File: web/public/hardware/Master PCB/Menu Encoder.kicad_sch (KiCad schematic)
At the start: 7 parts, among them SW2 Menu Encoder

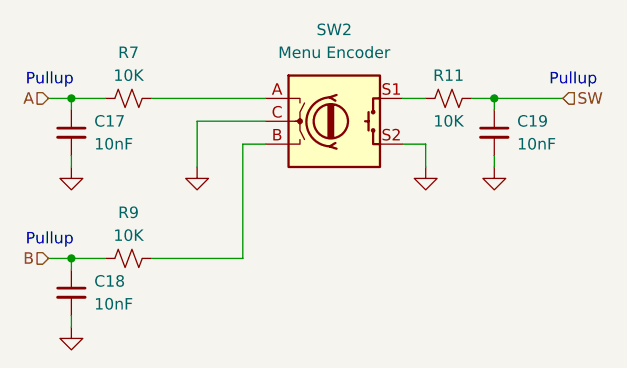
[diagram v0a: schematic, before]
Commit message: Add LED level shifters
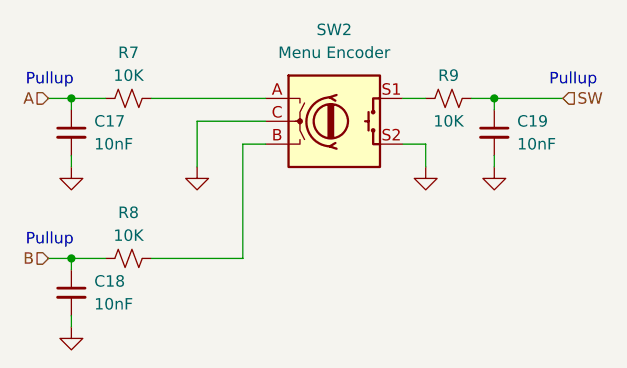
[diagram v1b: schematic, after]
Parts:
- renumbered R9 to R8, R11 to R9
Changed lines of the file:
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@@
   (symbol (lib_id "Device:R_Small_US") (at 152.4 91.44 90) (unit 1)
     (in_bom yes) (on_board yes) (dnp no)
-    (property "Reference" "R11" (at 152.4 88.9 90)
+    (property "Reference" "R9" (at 152.4 88.9 90)
       (effects (font (size 1.27 1.27)))
     )
@@
       (project "Master PCB"
         (path "/61606422-4f73-4717-9ce6-6ac5e634e7ae/41b61d17-0f73-40ac-8928-223428bb5236"
-          (reference "R11") (unit 1)
+          (reference "R9") (unit 1)
         )
       )
@@
   (symbol (lib_id "Device:R_Small_US") (at 116.84 109.22 90) (unit 1)
     (in_bom yes) (on_board yes) (dnp no)
-    (property "Reference" "R9" (at 116.84 104.14 90)
+    (property "Reference" "R8" (at 116.84 104.14 90)
       (effects (font (size 1.27 1.27)))
     )
@@
       (project "Master PCB"
         (path "/61606422-4f73-4717-9ce6-6ac5e634e7ae/41b61d17-0f73-40ac-8928-223428bb5236"
-          (reference "R9") (unit 1)
+          (reference "R8") (unit 1)
         )
       )

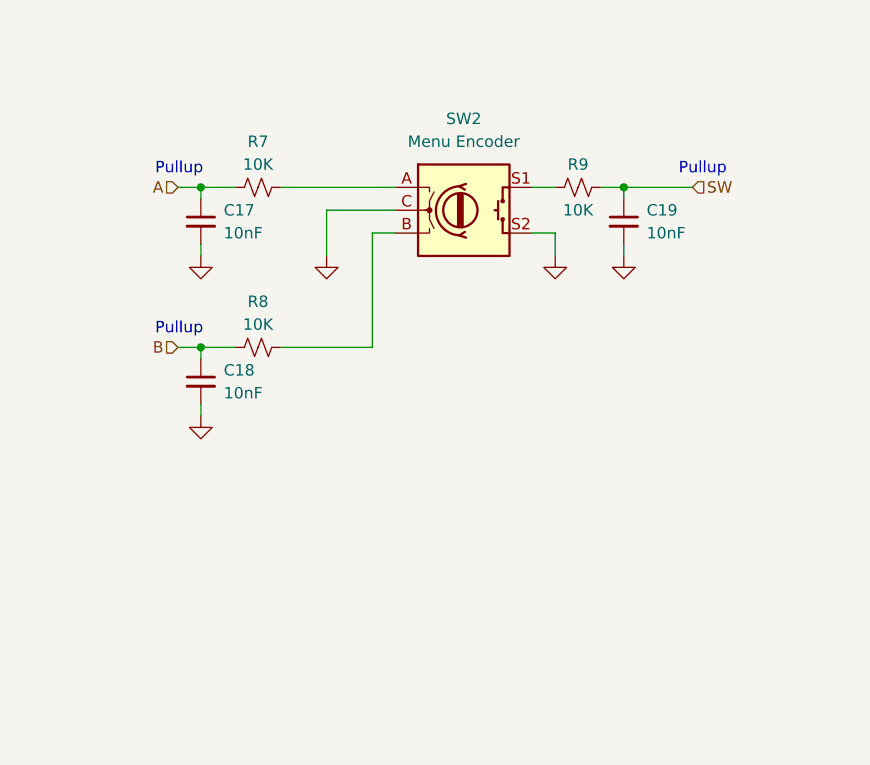
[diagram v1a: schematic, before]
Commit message: Finish schematic and start routing PCB
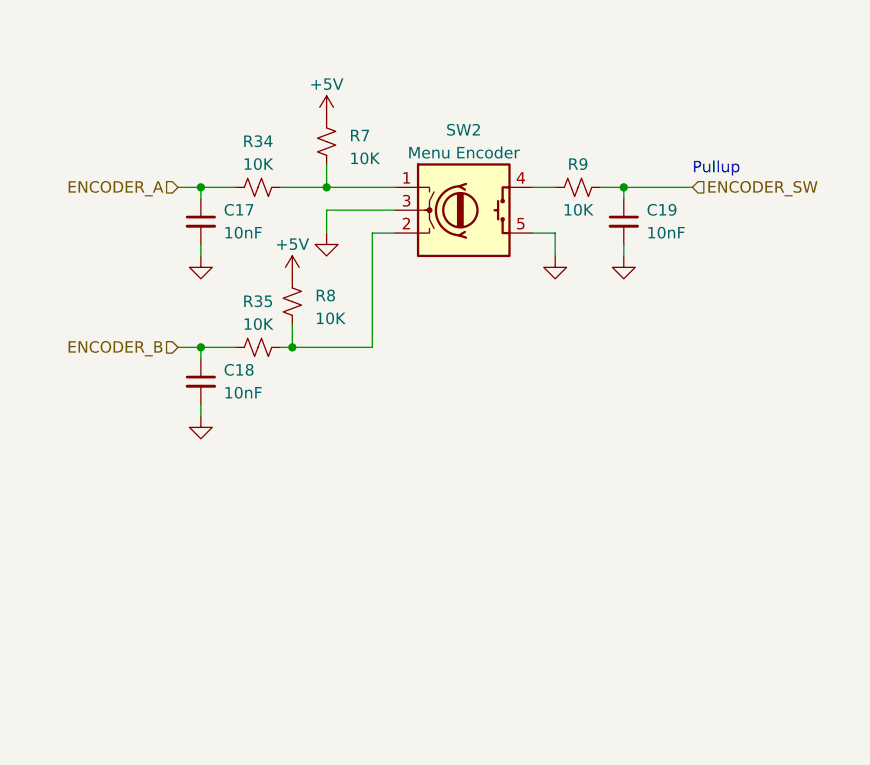
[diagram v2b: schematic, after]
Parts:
- removed SW2: Menu Encoder, symbol Device:RotaryEncoder_Switch
- added R34, R35: 10K, Resistor_SMD:R_0805_2012Metric_Pad1.20x1.40mm_HandSolder, symbol Device:R_Small_US
- added SW2: Menu Encoder, Connector_PinHeader_2.54mm:PinHeader_1x05_P2.54mm_Vertical, symbol Device_Custom:RotaryEncoder_Switch
- C17, C18, C19: footprint (none) -> Capacitor_SMD:C_0805_2012Metric_Pad1.18x1.45mm_HandSolder
- R7, R8, R9: footprint (none) -> Resistor_SMD:R_0805_2012Metric_Pad1.20x1.40mm_HandSolder
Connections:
- net GND: now also SW2.3 (C), SW2.5 (S2)
- net at R9.1: now also SW2.4 (S1)
- net at R8.2: now also R35.2, SW2.2 (B)
- net at R7.2: now also R34.2, SW2.1 (A)
- net A renamed +5V
- net +5V: now also R8.1; no longer C17.1
- net B renamed ENCODER_B
- net ENCODER_B: now also R35.1; no longer R8.1
- net SW renamed ENCODER_SW
- new net ENCODER_A: C17.1, R34.1

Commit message: Add ESD ICs and route part of board
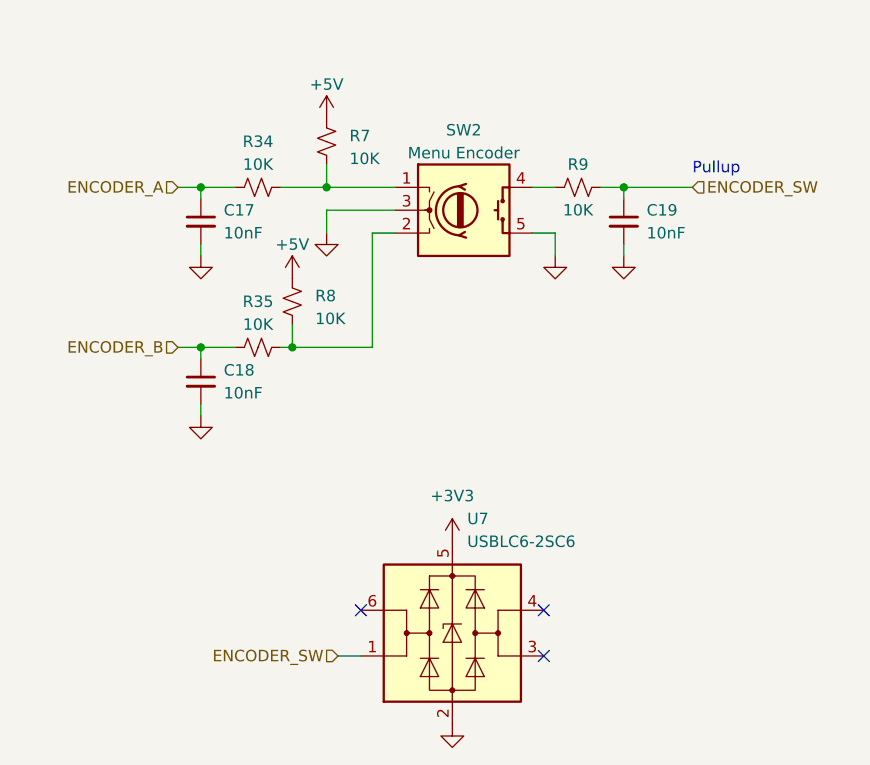
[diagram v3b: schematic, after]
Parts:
- added U7: USBLC6-2SC6, Package_TO_SOT_SMD:SOT-23-6, symbol Power_Protection:USBLC6-2SC6
- SW2: footprint Connector_PinHeader_2.54mm:PinHeader_1x05_P2.54mm_Vertical -> Connector_JST:JST_PH_B5B-PH-K_1x05_P2.00mm_Vertical
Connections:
- net ENCODER_SW: now also U7.1 (I/O1)
- net GND: now also U7.2 (GND)
- new net +3V3: U7.5 (VBUS)
- no-connect marks 0 -> 3
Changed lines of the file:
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@@
   (junction (at 124.46 91.44) (diameter 0) (color 0 0 0 0)
   )
+  (no_connect (at 148.59 138.43))
+  (no_connect (at 128.27 138.43))
+  (no_connect (at 148.59 143.51))
   (wire (pts (xy 124.46 93.98) (xy 132.08 93.98))
     (stroke (width 0) (type default))
@@
   )
   (wire (pts (xy 129.54 96.52) (xy 132.08 96.52))
+    (stroke (width 0) (type default))
+  )
+  (wire (pts (xy 125.73 143.51) (xy 128.27 143.51))
     (stroke (width 0) (type default))
   )
@@
     (effects (font (size 1.27 1.27)) (justify left))
   )
+  (hierarchical_label "ENCODER_SW" (shape input) (at 125.73 143.51 180) (fields_autoplaced)
+    (effects (font (size 1.27 1.27)) (justify right))
+  )
   (hierarchical_label "ENCODER_A" (shape input) (at 107.95 91.44 180) (fields_autoplaced)
     (effects (font (size 1.27 1.27)) (justify right))
+  )
+  (symbol (lib_id "power:GND") (at 138.43 151.13 0) (unit 1)
+    (in_bom yes) (on_board yes) (dnp no) (fields_autoplaced)
+    (property "Reference" "#PWR083" (at 138.43 157.48 0)
+      (effects (font (size 1.27 1.27)) hide)
+    )
+    (property "Value" "GND" (at 138.43 156.21 0)
+      (effects (font (size 1.27 1.27)) hide)
+    )
+    (property "Footprint" "" (at 138.43 151.13 0)
+      (effects (font (size 1.27 1.27)) hide)
+    )
+    (property "Datasheet" "" (at 138.43 151.13 0)
+      (effects (font (size 1.27 1.27)) hide)
+    )
+    (pin "1")
+    (instances
+      (project "Master PCB"
+        (path "/61606422-4f73-4717-9ce6-6ac5e634e7ae"
+          (reference "#PWR083") (unit 1)
+        )
+        (path "/61606422-4f73-4717-9ce6-6ac5e634e7ae/41b61d17-0f73-40ac-8928-223428bb5236"
+          (reference "#PWR085") (unit 1)
+        )
+      )
+    )
   )
   (symbol (lib_id "Device:R_Small_US") (at 152.4 91.44 90) (unit 1)
@@
       (effects (font (size 1.27 1.27)))
     )
-    (property "Footprint" "Connector_PinHeader_2.54mm:PinHeader_1x05_P2.54mm_Vertical" (at 135.89 89.916 0)
+    (property "Footprint" "Connector_JST:JST_PH_B5B-PH-K_1x05_P2.00mm_Vertical" (at 135.89 89.916 0)
       (effects (font (size 1.27 1.27)) hide)
     )
@@
     )
   )
+  (symbol (lib_id "power:+3V3") (at 138.43 130.81 0) (unit 1)
+    (in_bom yes) (on_board yes) (dnp no) (fields_autoplaced)
+    (property "Reference" "#PWR082" (at 138.43 134.62 0)
+      (effects (font (size 1.27 1.27)) hide)
+    )
+    (property "Value" "+3V3" (at 138.43 125.73 0)
+      (effects (font (size 1.27 1.27)))
+    )
+    (property "Footprint" "" (at 138.43 130.81 0)
+      (effects (font (size 1.27 1.27)) hide)
+    )
+    (property "Datasheet" "" (at 138.43 130.81 0)
+      (effects (font (size 1.27 1.27)) hide)
+    )
+    (pin "1")
+    (instances
+      (project "Master PCB"
+        (path "/61606422-4f73-4717-9ce6-6ac5e634e7ae"
+          (reference "#PWR082") (unit 1)
+        )
+        (path "/61606422-4f73-4717-9ce6-6ac5e634e7ae/41b61d17-0f73-40ac-8928-223428bb5236"
+          (reference "#PWR084") (unit 1)
+        )
+      )
+    )
+  )
   (symbol (lib_id "power:GND") (at 157.48 99.06 0) (unit 1)
     (in_bom yes) (on_board yes) (dnp no) (fields_autoplaced)
@@
         )
       )
+    )
+  )
+  (symbol (lib_id "Power_Protection:USBLC6-2SC6") (at 138.43 140.97 0) (unit 1)
+    (in_bom yes) (on_board yes) (dnp no) (fields_autoplaced)
+    (property "Reference" "U7" (at 140.0811 128.27 0)
+      (effects (font (size 1.27 1.27)) (justify left))
+    )
+    (property "Value" "USBLC6-2SC6" (at 140.0811 130.81 0)
+      (effects (font (size 1.27 1.27)) (justify left))
+    )
+    (property "Footprint" "Package_TO_SOT_SMD:SOT-23-6" (at 138.43 153.67 0)
+      (effects (font (size 1.27 1.27)) hide)
+    )
+    (property "Datasheet" "https://www.st.com/resource/en/datasheet/usblc6-2.pdf" (at 143.51 132.08 0)
+      (effects (font (size 1.27 1.27)) hide)
+    )
+    (pin "1")
+    (pin "2")
+    (pin "3")
+    (pin "4")
+    (pin "5")
+    (pin "6")
+    (instances
+      (project "Master PCB"
+        (path "/61606422-4f73-4717-9ce6-6ac5e634e7ae"
+          (reference "U7") (unit 1)
+        )
+        (path "/61606422-4f73-4717-9ce6-6ac5e634e7ae/41b61d17-0f73-40ac-8928-223428bb5236"
+          (reference "U8") (unit 1)
+        )
+      )

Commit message: Fix encoder resistor values
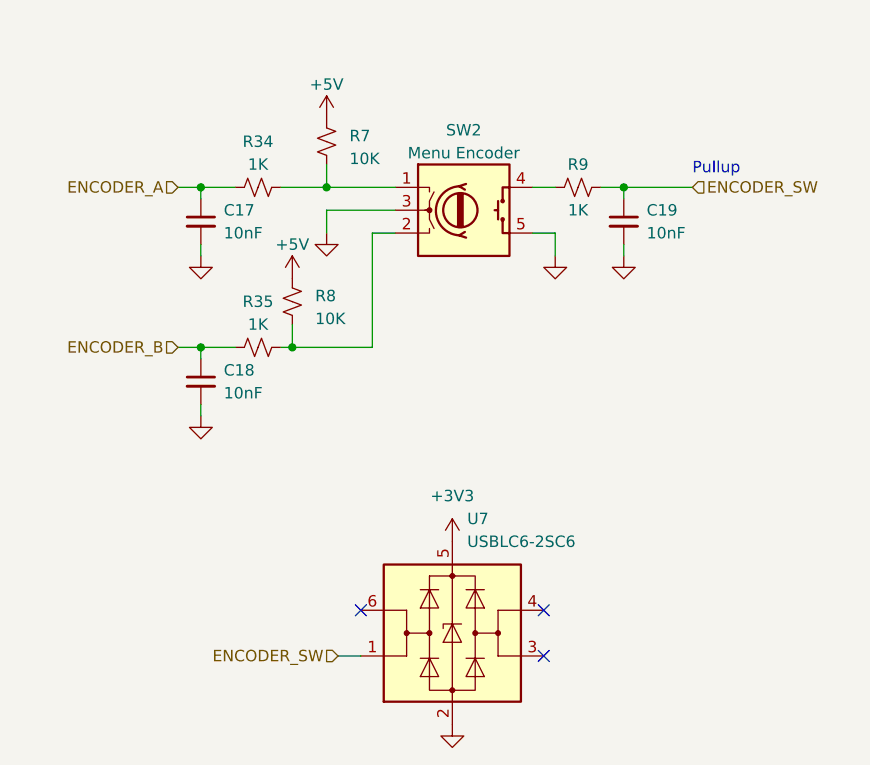
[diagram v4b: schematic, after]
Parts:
- R34, R35, R9: value 10K -> 1K
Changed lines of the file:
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@@
       (effects (font (size 1.27 1.27)))
     )
-    (property "Value" "10K" (at 152.4 93.98 90)
+    (property "Value" "1K" (at 152.4 93.98 90)
       (effects (font (size 1.27 1.27)))
     )
@@
       (effects (font (size 1.27 1.27)))
     )
-    (property "Value" "10K" (at 116.84 88.9 90)
+    (property "Value" "1K" (at 116.84 88.9 90)
       (effects (font (size 1.27 1.27)))
     )
@@
   )
   (symbol (lib_id "Device:R_Small_US") (at 116.84 109.22 90) (unit 1)
-    (in_bom yes) (on_board yes) (dnp no) (fields_autoplaced)
+    (in_bom yes) (on_board yes) (dnp no)
     (property "Reference" "R35" (at 116.84 104.14 90)
       (effects (font (size 1.27 1.27)))
     )
-    (property "Value" "10K" (at 116.84 106.68 90)
-      (effects (font (size 1.27 1.27)))
-    )
+    (property "Value" "1K" (at 116.84 106.68 90)
+      (effects (font (size 1.27 1.27)))
+    )

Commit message: Miscellaneous cleanup
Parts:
- removed U7: USBLC6-2SC6, Package_TO_SOT_SMD:SOT-23-6, symbol Power_Protection:USBLC6-2SC6
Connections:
- no-connect marks 3 -> 0
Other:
- note added: "Rotary encoder for table"
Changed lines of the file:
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@@
   (junction (at 124.46 91.44) (diameter 0) (color 0 0 0 0)
   )
-  (no_connect (at 148.59 138.43))
-  (no_connect (at 128.27 138.43))
-  (no_connect (at 148.59 143.51))
   (wire (pts (xy 124.46 93.98) (xy 132.08 93.98))
     (stroke (width 0) (type default))
@@
     (stroke (width 0) (type default))
   )
-  (wire (pts (xy 125.73 143.51) (xy 128.27 143.51))
-    (stroke (width 0) (type default))
-  )
   (wire (pts (xy 147.32 96.52) (xy 149.86 96.52))
     (stroke (width 0) (type default))
@@
   (wire (pts (xy 110.49 91.44) (xy 110.49 92.71))
     (stroke (width 0) (type default))
+  )
+  (rectangle (start 90.17 74.93) (end 182.88 123.19)
+    (stroke (width 0) (type default))
+    (fill (type none))
+  )
+  (text "Rotary encoder for table" (at 90.17 74.93 0)
+    (effects (font (size 1.27 1.27)) (justify left bottom))
   )
   (text "Pullup" (at 165.1 90.17 0)
@@
     (effects (font (size 1.27 1.27)) (justify left))
   )
-  (hierarchical_label "ENCODER_SW" (shape input) (at 125.73 143.51 180) (fields_autoplaced)
-    (effects (font (size 1.27 1.27)) (justify right))
-  )
   (hierarchical_label "ENCODER_A" (shape input) (at 107.95 91.44 180) (fields_autoplaced)
     (effects (font (size 1.27 1.27)) (justify right))
-  )
-  (symbol (lib_id "power:GND") (at 138.43 151.13 0) (unit 1)
-    (in_bom yes) (on_board yes) (dnp no) (fields_autoplaced)
-    (property "Reference" "#PWR083" (at 138.43 157.48 0)
-      (effects (font (size 1.27 1.27)) hide)
-    )
-    (property "Value" "GND" (at 138.43 156.21 0)
-      (effects (font (size 1.27 1.27)) hide)
-    )
-    (property "Footprint" "" (at 138.43 151.13 0)
-      (effects (font (size 1.27 1.27)) hide)
-    )
-    (property "Datasheet" "" (at 138.43 151.13 0)
-      (effects (font (size 1.27 1.27)) hide)
-    )
-    (pin "1")
-    (instances
-      (project "Master PCB"
-        (path "/61606422-4f73-4717-9ce6-6ac5e634e7ae"
-          (reference "#PWR083") (unit 1)
-        )
-        (path "/61606422-4f73-4717-9ce6-6ac5e634e7ae/41b61d17-0f73-40ac-8928-223428bb5236"
-          (reference "#PWR085") (unit 1)
-        )
-      )
-    )
   )
   (symbol (lib_id "Device:R_Small_US") (at 152.4 91.44 90) (unit 1)
@@
     )
   )
-  (symbol (lib_id "power:+3V3") (at 138.43 130.81 0) (unit 1)
-    (in_bom yes) (on_board yes) (dnp no) (fields_autoplaced)
-    (property "Reference" "#PWR082" (at 138.43 134.62 0)
-      (effects (font (size 1.27 1.27)) hide)
-    )
-    (property "Value" "+3V3" (at 138.43 125.73 0)
-      (effects (font (size 1.27 1.27)))
-    )
-    (property "Footprint" "" (at 138.43 130.81 0)
-      (effects (font (size 1.27 1.27)) hide)
-    )
-    (property "Datasheet" "" (at 138.43 130.81 0)
-      (effects (font (size 1.27 1.27)) hide)
-    )
-    (pin "1")
-    (instances
-      (project "Master PCB"
-        (path "/61606422-4f73-4717-9ce6-6ac5e634e7ae"
-          (reference "#PWR082") (unit 1)
-        )
-        (path "/61606422-4f73-4717-9ce6-6ac5e634e7ae/41b61d17-0f73-40ac-8928-223428bb5236"
-          (reference "#PWR084") (unit 1)
-        )
-      )
-    )
-  )
   (symbol (lib_id "power:GND") (at 157.48 99.06 0) (unit 1)
     (in_bom yes) (on_board yes) (dnp no) (fields_autoplaced)
@@
         )
       )
-    )
-  )
-  (symbol (lib_id "Power_Protection:USBLC6-2SC6") (at 138.43 140.97 0) (unit 1)
-    (in_bom yes) (on_board yes) (dnp no) (fields_autoplaced)
-    (property "Reference" "U7" (at 140.0811 128.27 0)
-      (effects (font (size 1.27 1.27)) (justify left))
-    )
-    (property "Value" "USBLC6-2SC6" (at 140.0811 130.81 0)
-      (effects (font (size 1.27 1.27)) (justify left))
-    )
-    (property "Footprint" "Package_TO_SOT_SMD:SOT-23-6" (at 138.43 153.67 0)
-      (effects (font (size 1.27 1.27)) hide)
-    )
-    (property "Datasheet" "https://www.st.com/resource/en/datasheet/usblc6-2.pdf" (at 143.51 132.08 0)
-      (effects (font (size 1.27 1.27)) hide)
-    )
-    (pin "1")
-    (pin "2")
-    (pin "3")
-    (pin "4")
-    (pin "5")
-    (pin "6")
-    (instances
-      (project "Master PCB"
-        (path "/61606422-4f73-4717-9ce6-6ac5e634e7ae"
-          (reference "U7") (unit 1)
-        )
-        (path "/61606422-4f73-4717-9ce6-6ac5e634e7ae/41b61d17-0f73-40ac-8928-223428bb5236"
-          (reference "U8") (unit 1)
-        )
-      )

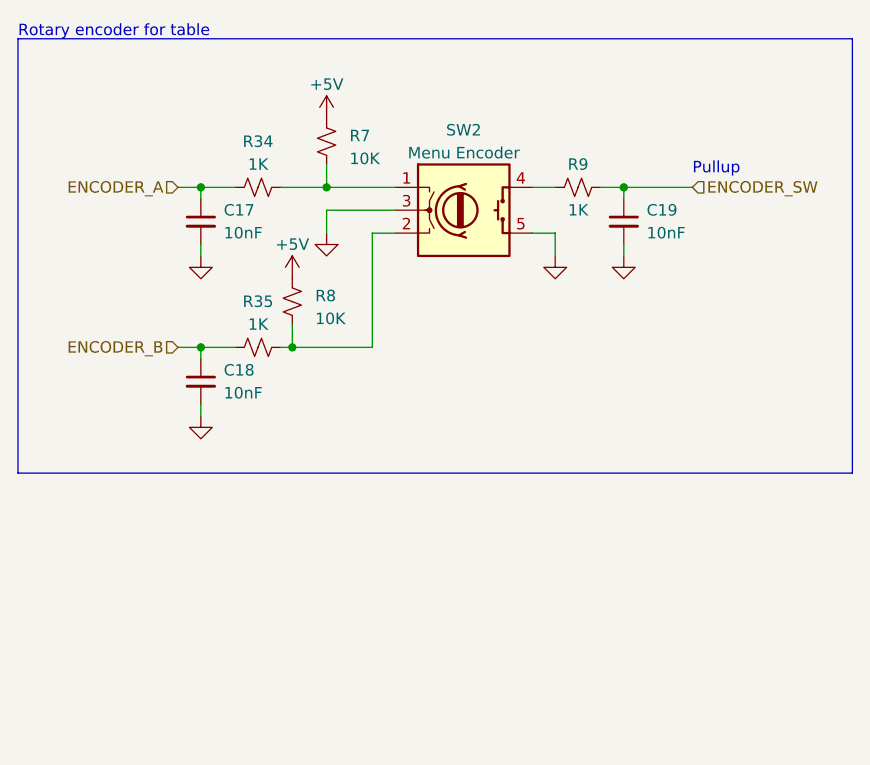
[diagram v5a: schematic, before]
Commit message: Fix encoder schematic and miscellaneous cleanup (new date, etc.)
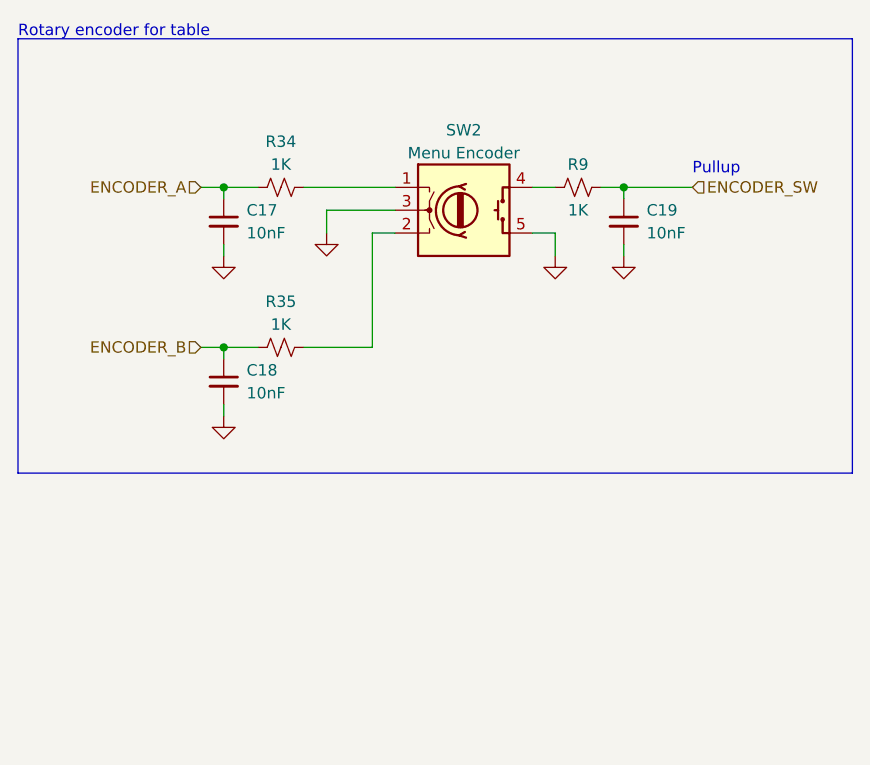
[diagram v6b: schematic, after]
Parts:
- removed R7, R8: 10K, Resistor_SMD:R_0805_2012Metric_Pad1.20x1.40mm_HandSolder, symbol Device:R_Small_US
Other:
- moved on the sheet: C17, C18, R34, R35

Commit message: More misc. cleanup and generate updated production files
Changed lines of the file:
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@@
     (stroke (width 0) (type default))
   )
-  (rectangle (start 90.17 74.93) (end 182.88 123.19)
+  (rectangle (start 90.17 80.01) (end 182.88 123.19)
     (stroke (width 0) (type default))
     (fill (type none))
   )
-  (text "Rotary encoder for table" (at 90.17 74.93 0)
+  (text "Rotary encoder for table" (at 90.17 80.01 0)
     (effects (font (size 1.27 1.27)) (justify left bottom))
   )
